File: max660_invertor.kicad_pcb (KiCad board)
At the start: 2 copper layers, 12 x 17 mm, 5 parts, among them U1 MAX660

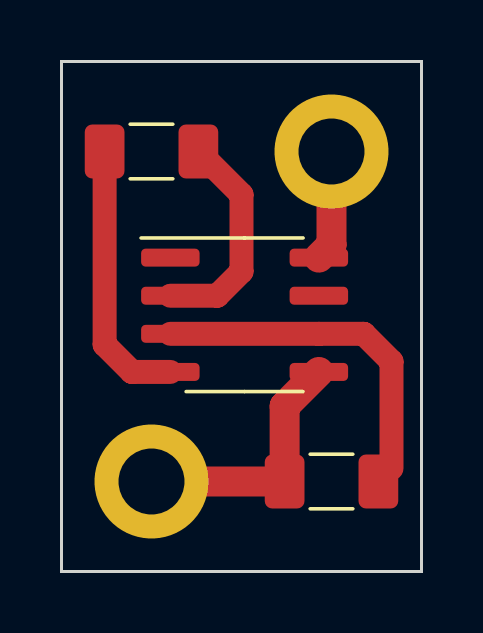
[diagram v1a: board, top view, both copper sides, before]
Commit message: add labels
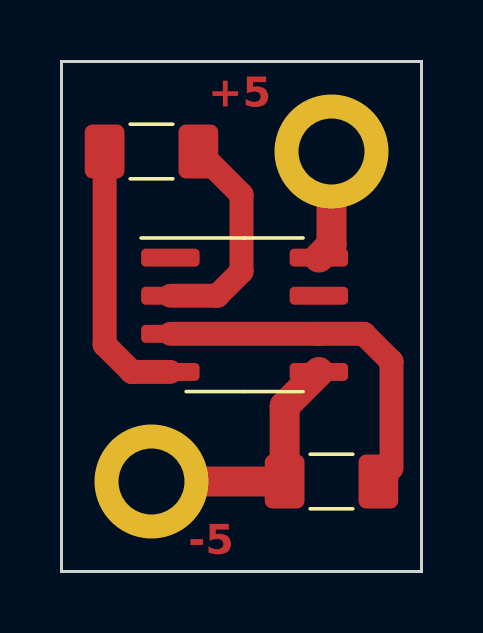
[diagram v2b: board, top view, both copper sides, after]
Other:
- board text added: "+5"
- board text added: "-5"
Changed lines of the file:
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@@
 		(layer "Edge.Cuts")
+	)
+	(gr_text "+5"
+		(at 145.884627 79.621867 0)
+		(layer "F.Cu")
+		(effects
+			(font
+				(size 1 1)
+				(thickness 0.25)
+				(bold yes)
+			)
+			(justify left bottom)
+		)
+	)
+	(gr_text "-5"
+		(at 145.223665 94.534815 0)
+		(layer "F.Cu")
+		(effects
+			(font
+				(size 1 1)
+				(thickness 0.25)
+				(bold yes)
+			)
+			(justify left bottom)
+		)
 	)
 	(segment
